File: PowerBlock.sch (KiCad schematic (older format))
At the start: 0 parts

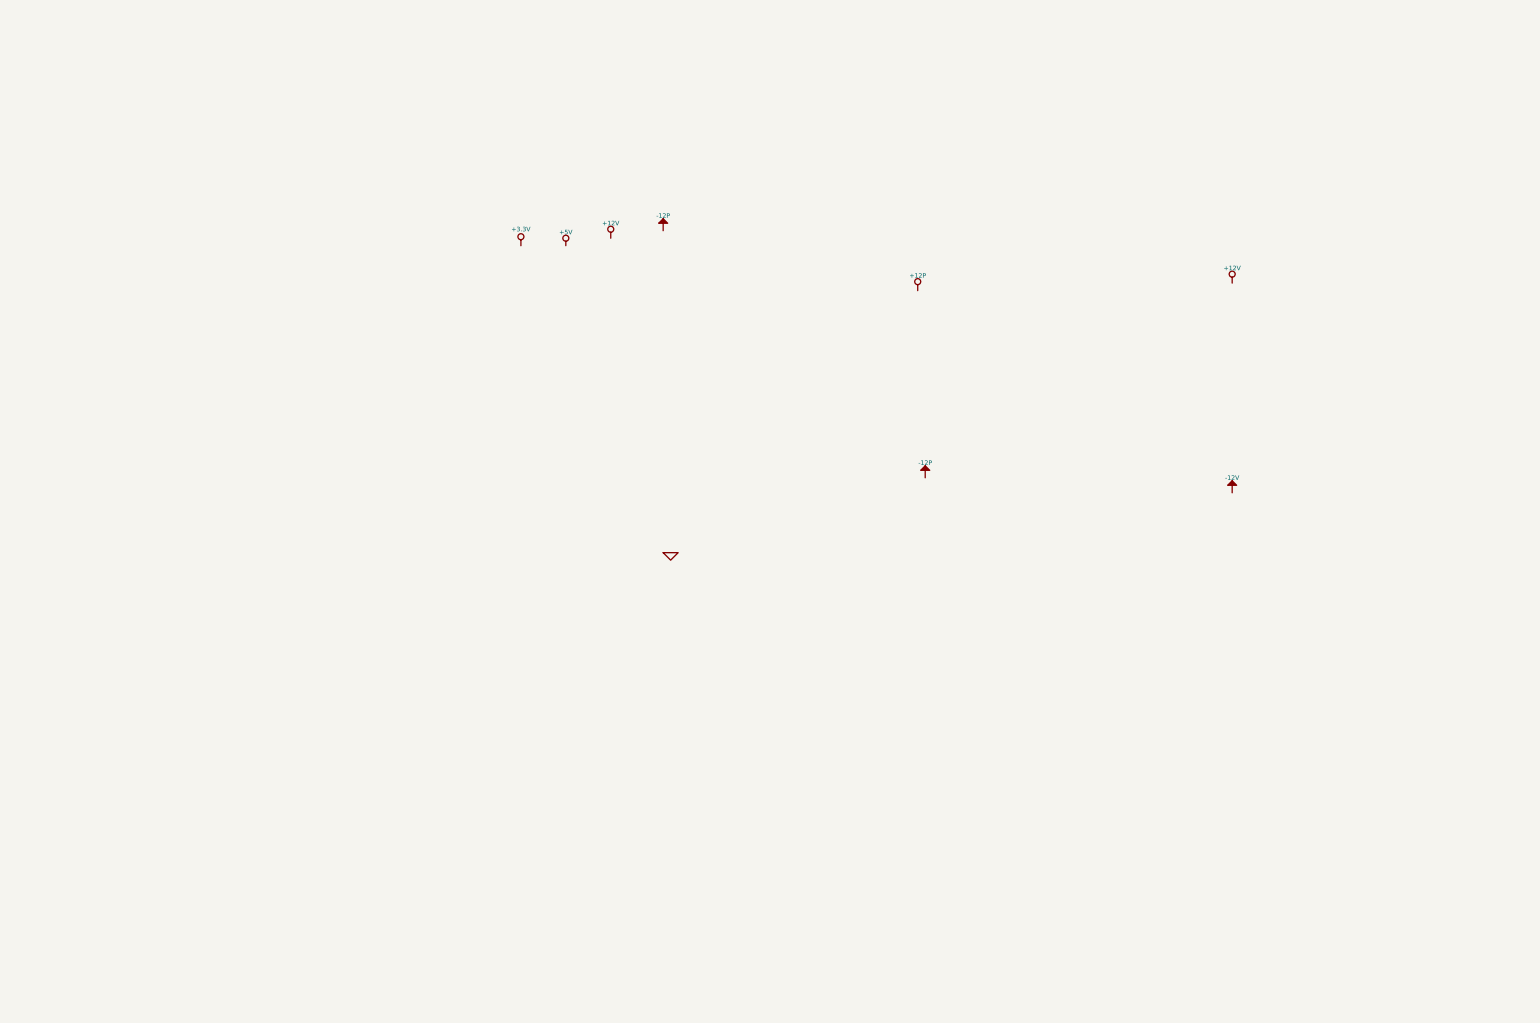
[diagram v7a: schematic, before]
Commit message: Added contents to Power Supply and monitor block
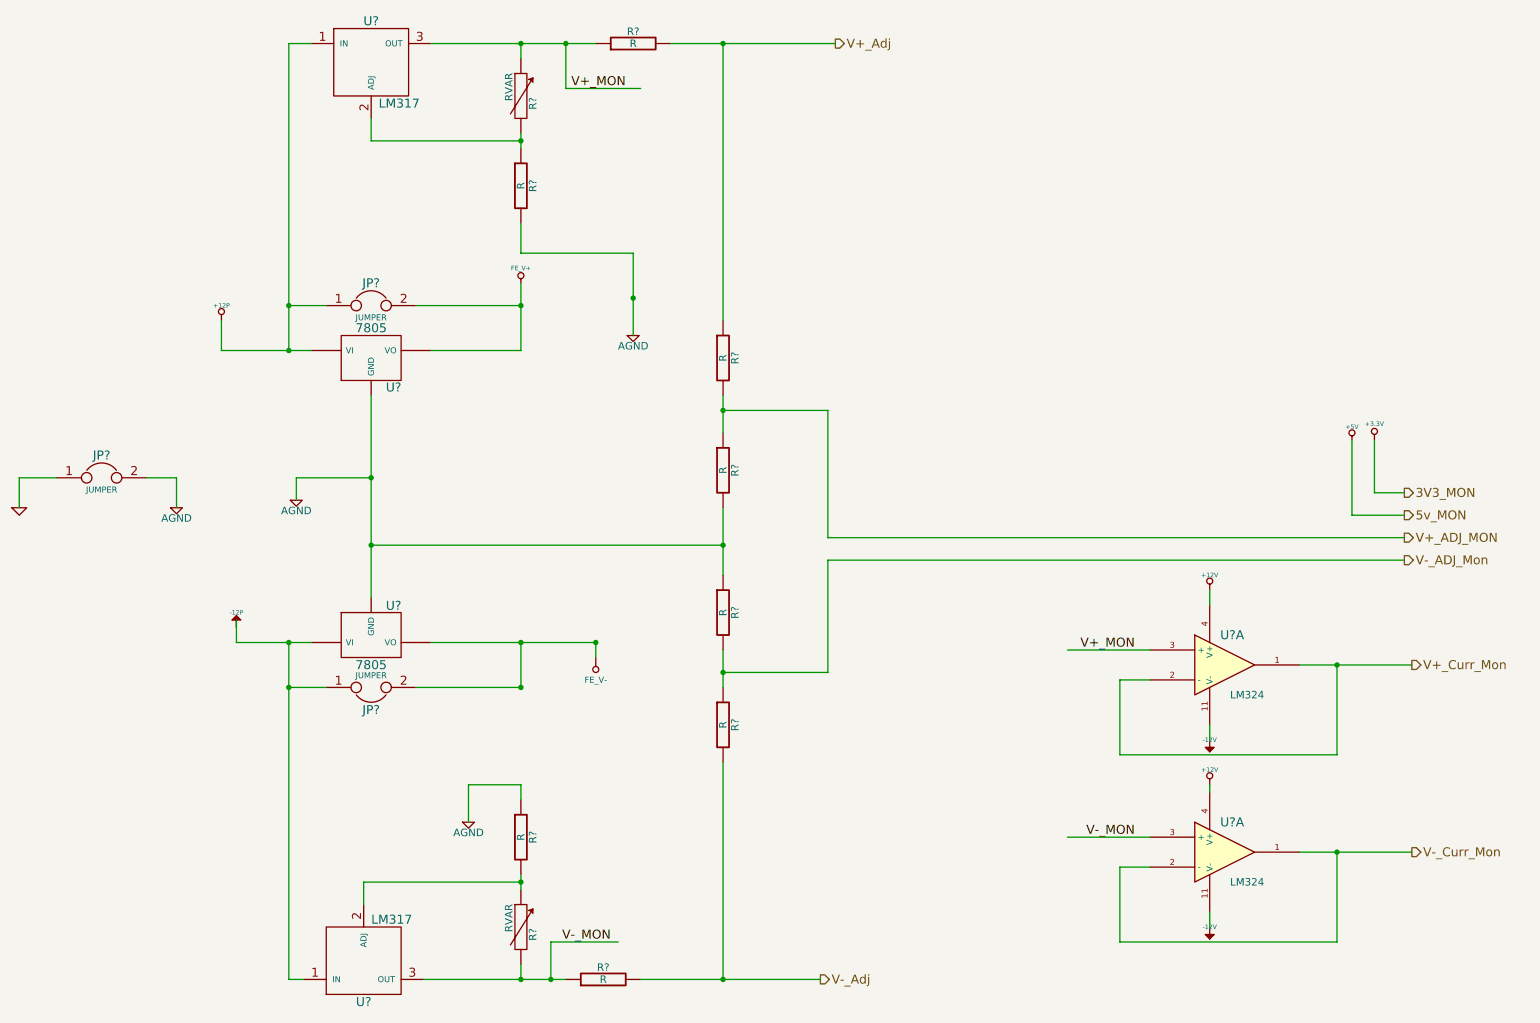
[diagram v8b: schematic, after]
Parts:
- added JP? (x3): JUMPER, symbol JUMPER
- added R? (x8): R, symbol R
- added R? (x2): RVAR, symbol RVAR
- added U? (x2): LM317, symbol LM317
- added U? (x2): 7805, symbol 7805
- added U? (x2): LM324, symbol LM324
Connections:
- net labels added: 3V3_MON, 5v_MON, AGND, FE_V+, FE_V-, V+_ADJ_MON, V+_Adj, V+_Curr_Mon, V+_MON, V-_ADJ_Mon, V-_Adj, V-_Curr_Mon, V-_MON
- wire segments 0 -> 100
